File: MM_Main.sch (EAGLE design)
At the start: 81 parts, among them IC1 ULN2003AD, IC2 TB6612FNG, IC4 LD117ADT50TR, IC5 MCP1825, Q1 TEFT4300, Q2 TEFT4300, Q3 TEFT4300, Q4 TEFT4300, Q5 TEFT4300, Q6 TEFT4300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

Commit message: schamat kodu z CubeMX
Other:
- note added: "L"
- note added: "LF"
- note added: "LS"
- note added: "R"
- note added: "RF"
- note added: "RS"
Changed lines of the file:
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@@
 RF - Right Front
 </text>
+<text x="93.98" y="-48.26" size="1.778" layer="91">L</text>
+<text x="91.44" y="-48.26" size="1.778" layer="91">R</text>
+<text x="88.9" y="-45.72" size="1.778" layer="91" rot="R270">RF</text>
+<text x="86.36" y="-45.72" size="1.778" layer="91" rot="R270">RS</text>
+<text x="139.7" y="-17.78" size="1.778" layer="91">LS</text>
+<text x="109.22" y="-53.34" size="1.778" layer="91" rot="R90">LF</text>
 </plain>
 <instances>

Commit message: poprawione przyciski, kwarc i wylacznik zasilania
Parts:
- removed BT0, BT1, RST_BTN: TACTILE-SWITCH-7914G, GeekAmmo:TACTILE-SWITCH-7914G
- removed ZAS: (no value), special:SW_DIP-1
- added Q8: 8MHz, _microMouse:CRYSTAL_5X3.2MM
- added S1: TL32PO, switch:TL32PO
- added S2, S3: DTS-3, switch-tact:DTS-3
- added S4: DTSM-6, switch-tact:DTSM-6
- added S5: DTSM-3, switch-tact:DTSM-3
- added U$2: CRYSTAL_5X3.2MM, _microMouse:CRYSTAL_5X3.2MM
- C_OSC1, C_OSC2: value 27p -> 33p
- LED4: value green -> blue
- LED6: value yellow -> blue
- R10, R12, R13: value 10K -> 150R
- R11: value 10K -> 10k
- R20, R27: value 10K -> 33R
- R25: value (none) -> 10k
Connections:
- net +3V3: now also S3.1; no longer BT0.3
- net BTN: now also S2.1; no longer BT1.3
- net GND: now also S5.1; no longer RST_BTN.3
- net N$23: now also S3.2; no longer BT0.1
- net N$24: now also S1.P; no longer ZAS.2
- net N$29: now also S2.2; no longer BT1.1
- net N$9: now also S1.S; no longer ZAS.1
- net OSC_IN: now also Q8.2; no longer Q7.2
- net OSC_OUT: now also Q8.1; no longer Q7.1
- net RST: now also S5.2; no longer RST_BTN.1
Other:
- note removed: "L"
- note removed: "LF"
- note removed: "LS"
- note removed: "R"
- note removed: "RF"
- note removed: "RS"
- moved on the sheet: Q7

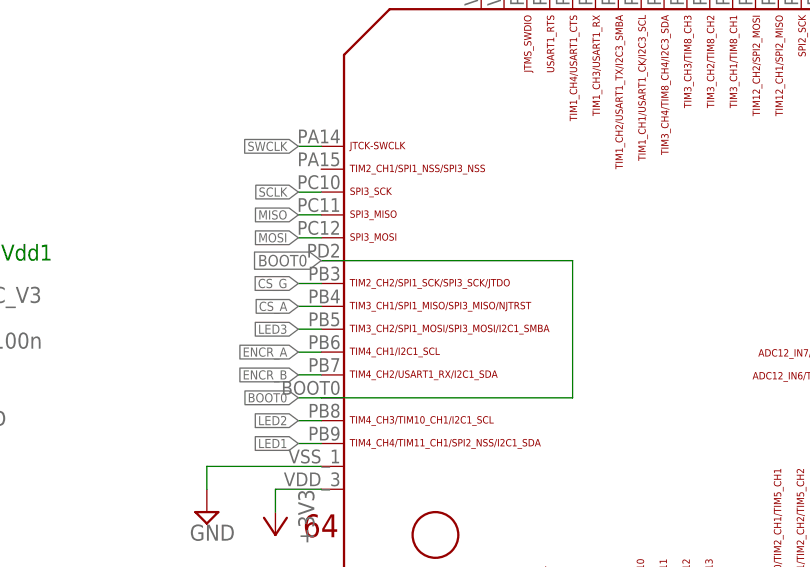
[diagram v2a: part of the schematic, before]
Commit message: PD2 zamienione z PA15
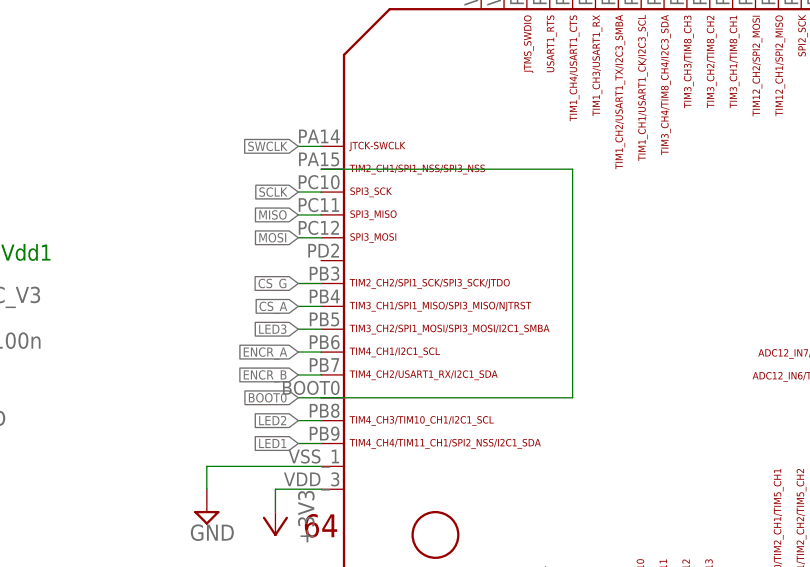
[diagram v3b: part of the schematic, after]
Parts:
- removed U$2: CRYSTAL_5X3.2MM, _microMouse:CRYSTAL_5X3.2MM
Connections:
- net BOOT0: now also U$6.PA15; no longer U$6.PD2
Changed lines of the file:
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@@
 <part name="+3V29" library="supply1" deviceset="+3V3" device=""/>
 <part name="R26" library="rcl" deviceset="R-EU_" device="R0805"/>
-<part name="U$2" library="_microMouse" deviceset="CRYSTAL_5X3.2MM" device=""/>
 <part name="Q8" library="_microMouse" deviceset="CRYSTAL_5X3.2MM" device="" value="8MHz"/>
 <part name="S1" library="switch" deviceset="TL32PO" device=""/>
@@
 <label x="48.26" y="-7.62" size="1.016" layer="95" rot="R180" xref="yes"/>
 <pinref part="U$6" gate="G$1" pin="BOOT0"/>
-<pinref part="U$6" gate="G$1" pin="PD2"/>
-<wire x1="50.8" y1="7.62" x2="78.74" y2="7.62" width="0.1524" layer="91"/>
-<wire x1="78.74" y1="7.62" x2="78.74" y2="-7.62" width="0.1524" layer="91"/>
 <wire x1="78.74" y1="-7.62" x2="50.8" y2="-7.62" width="0.1524" layer="91"/>
-<label x="50.8" y="7.62" size="1.27" layer="95" rot="R180" xref="yes"/>
-</segment>
-</net>
+<pinref part="U$6" gate="G$1" pin="PA15"/>
+<wire x1="78.74" y1="-7.62" x2="78.74" y2="17.78" width="0.1524" layer="91"/>
+<wire x1="78.74" y1="17.78" x2="50.8" y2="17.78" width="0.1524" layer="91"/>
+</segment>
+</net>

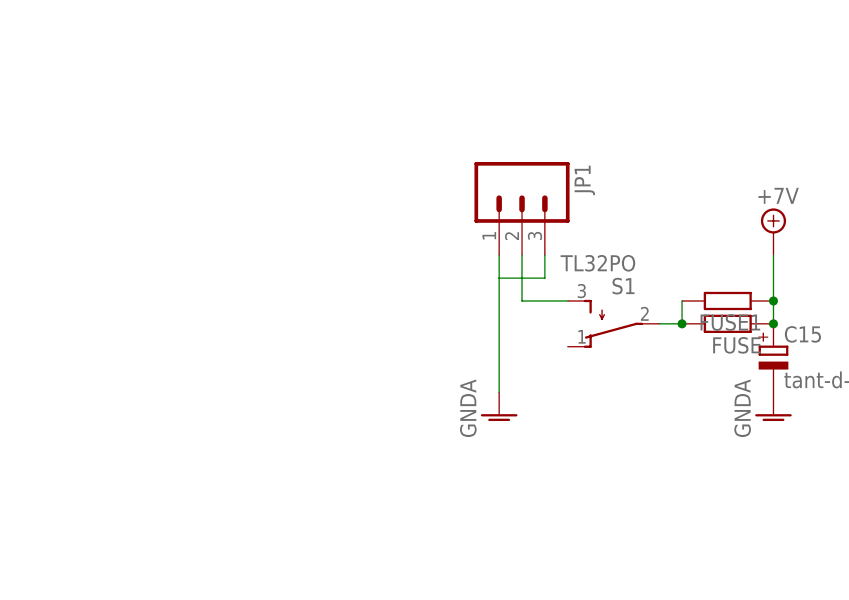
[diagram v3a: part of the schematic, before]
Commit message: dodany suwak i miejsce na 2 lipo
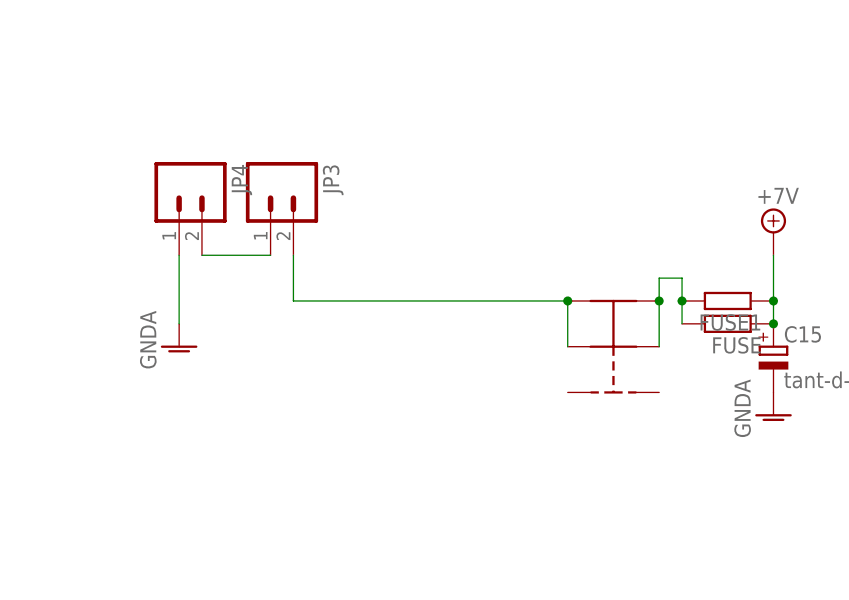
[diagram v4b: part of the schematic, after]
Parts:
- removed JP1: (no value), SparkFun-Connectors:M03POLAR
- removed S1: TL32PO, switch:TL32PO
- added JP3, JP4: (no value), SparkFun_conn:M02POLAR
- added U$3: PRZELACZNIK_SUWAKOWY, _microMouse:PRZELACZNIK_SUWAKOWY
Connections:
- new net N$36: JP3.2, U$3.2, U$3.3
- net GNDA: now also JP4.1; no longer JP1.1, JP1.3
- net N$24: now also U$3.5, U$3.6; no longer S1.P
- net N$9: now also JP3.1, JP4.2; no longer JP1.2, S1.S
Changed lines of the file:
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@@
 <part name="U$6" library="_microMouse" deviceset="STM32F4X5" device=""/>
 <part name="AGND1" library="supply2" deviceset="GND" device=""/>
-<part name="JP1" library="SparkFun-Connectors" deviceset="M03" device="POLAR"/>
 <part name="R15" library="rcl" deviceset="R-EU_" device="R0805"/>
 <part name="D2" library="_microMouse" deviceset="SFH4545" device="-C" value="SFH4545-C"/>
@@
 <part name="R26" library="rcl" deviceset="R-EU_" device="R0805"/>
 <part name="Q8" library="_microMouse" deviceset="CRYSTAL_5X3.2MM" device="" value="8MHz"/>
-<part name="S1" library="switch" deviceset="TL32PO" device=""/>
 <part name="S2" library="switch-tact" deviceset="DTS-3" device=""/>
 <part name="S3" library="switch-tact" deviceset="DTS-3" device=""/>
 <part name="S4" library="switch-tact" deviceset="DTSM-6" device=""/>
 <part name="S5" library="switch-tact" deviceset="DTSM-3" device=""/>
+<part name="JP3" library="SparkFun_conn" deviceset="M02" device="POLAR"/>
+<part name="JP4" library="SparkFun_conn" deviceset="M02" device="POLAR"/>
+<part name="U$3" library="_microMouse" deviceset="PRZELACZNIK_SUWAKOWY" device=""/>
 </parts>
 <sheets>
@@
 <instance part="+3V21" gate="G$1" x="0" y="10.16" smashed="yes"/>
 <instance part="+3V22" gate="G$1" x="-12.7" y="10.16" smashed="yes"/>
-<instance part="GND4" gate="1" x="-152.4" y="111.76"/>
+<instance part="GND4" gate="1" x="-187.96" y="119.38"/>
 <instance part="GND10" gate="1" x="-88.9" y="134.62"/>
 <instance part="AGND17" gate="GND" x="-78.74" y="134.62"/>
@@
 <instance part="U$6" gate="G$1" x="86.36" y="0"/>
 <instance part="AGND1" gate="GND" x="96.52" y="-50.8"/>
-<instance part="JP1" gate="G$1" x="-149.86" y="137.16" rot="R270"/>
 <instance part="R15" gate="G$1" x="86.36" y="154.94" rot="R90"/>
 <instance part="D2" gate="G$1" x="86.36" y="144.78"/>
@@
 <instance part="R26" gate="G$1" x="-165.1" y="30.48" rot="R180"/>
 <instance part="Q8" gate="G$1" x="-10.16" y="-25.4" rot="R90"/>
-<instance part="S1" gate="BEF1" x="-139.7" y="121.92" rot="R90"/>
 <instance part="S2" gate="G$1" x="-63.5" y="55.88" rot="R90"/>
 <instance part="S3" gate="G$1" x="205.74" y="30.48" rot="R180"/>
 <instance part="S4" gate="G$1" x="256.54" y="12.7"/>
 <instance part="S5" gate="G$1" x="238.76" y="15.24"/>
+<instance part="JP3" gate="G$1" x="-177.8" y="137.16" rot="R270"/>
+<instance part="JP4" gate="G$1" x="-187.96" y="137.16" rot="R270"/>
+<instance part="U$3" gate="G$1" x="-139.7" y="119.38" rot="R90"/>
 </instances>
 <busses>
@@
 </segment>
 <segment>
-<wire x1="-152.4" y1="127" x2="-152.4" y2="129.54" width="0.1524" layer="91"/>
-<wire x1="-152.4" y1="127" x2="-147.32" y2="127" width="0.1524" layer="91"/>
-<wire x1="-147.32" y1="127" x2="-147.32" y2="129.54" width="0.1524" layer="91"/>
-<wire x1="-152.4" y1="127" x2="-152.4" y2="114.3" width="0.1524" layer="91"/>
 <pinref part="GND4" gate="1" pin="GNDA"/>
-<pinref part="JP1" gate="G$1" pin="1"/>
-<pinref part="JP1" gate="G$1" pin="3"/>
+<pinref part="JP4" gate="G$1" pin="1"/>
+<wire x1="-187.96" y1="121.92" x2="-187.96" y2="129.54" width="0.1524" layer="91"/>
 </segment>
 <segment>
@@
 <pinref part="FUSE" gate="G$1" pin="2"/>
 <pinref part="FUSE1" gate="G$1" pin="2"/>
-<pinref part="S1" gate="BEF1" pin="P"/>
-<wire x1="-132.08" y1="121.92" x2="-134.62" y2="121.92" width="0.1524" layer="91"/>
-<junction x="-132.08" y="121.92"/>
+<wire x1="-132.08" y1="124.46" x2="-132.08" y2="127" width="0.1524" layer="91"/>
+<wire x1="-132.08" y1="127" x2="-134.62" y2="127" width="0.1524" layer="91"/>
+<junction x="-132.08" y="124.46"/>
+<pinref part="U$3" gate="G$1" pin="6"/>
+<pinref part="U$3" gate="G$1" pin="5"/>
+<wire x1="-134.62" y1="124.46" x2="-134.62" y2="119.38" width="0.1524" layer="91"/>
+<wire x1="-134.62" y1="127" x2="-134.62" y2="124.46" width="0.1524" layer="91"/>
+<junction x="-134.62" y="124.46"/>
 </segment>
 </net>
@@
 </segment>
 </net>
-<net name="N$9" class="0">
-<segment>
-<wire x1="-149.86" y1="129.54" x2="-149.86" y2="124.46" width="0.1524" layer="91"/>
-<pinref part="JP1" gate="G$1" pin="2"/>
-<pinref part="S1" gate="BEF1" pin="S"/>
-<wire x1="-144.78" y1="124.46" x2="-149.86" y2="124.46" width="0.1524" layer="91"/>
-</segment>
-</net>
 <net name="INT_A" class="0">
 <segment>
@@
 </segment>
 </net>
+<net name="N$36" class="0">
+<segment>
+<pinref part="U$3" gate="G$1" pin="2"/>
+<pinref part="U$3" gate="G$1" pin="3"/>
+<wire x1="-144.78" y1="119.38" x2="-144.78" y2="124.46" width="0.1524" layer="91"/>
+<wire x1="-175.26" y1="124.46" x2="-144.78" y2="124.46" width="0.1524" layer="91"/>
+<junction x="-144.78" y="124.46"/>
+<pinref part="JP3" gate="G$1" pin="2"/>
+<wire x1="-175.26" y1="129.54" x2="-175.26" y2="124.46" width="0.1524" layer="91"/>
+</segment>
+</net>
+<net name="N$9" class="0">
+<segment>
+<pinref part="JP3" gate="G$1" pin="1"/>
+<pinref part="JP4" gate="G$1" pin="2"/>
+<wire x1="-177.8" y1="129.54" x2="-185.42" y2="129.54" width="0.1524" layer="91"/>
+</segment>
+</net>

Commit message: gerbery
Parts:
- removed Q7: 8MHz, crystal:CRYSTALCTS406
- removed S4: DTSM-6, switch-tact:DTSM-6
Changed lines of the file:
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@@
 <part name="C_V1" library="rcl" deviceset="C-EU" device="C0805" value="100n"/>
 <part name="C_V2" library="rcl" deviceset="C-EU" device="C0805" value="100n"/>
-<part name="Q7" library="crystal" deviceset="CRYSTAL" device="CTS406" value="8MHz"/>
 <part name="C_OSC1" library="rcl" deviceset="C-EU" device="C0805" value="33p"/>
 <part name="C_OSC2" library="rcl" deviceset="C-EU" device="C0805" value="33p"/>
@@
 <part name="S2" library="switch-tact" deviceset="DTS-3" device=""/>
 <part name="S3" library="switch-tact" deviceset="DTS-3" device=""/>
-<part name="S4" library="switch-tact" deviceset="DTSM-6" device=""/>
 <part name="S5" library="switch-tact" deviceset="DTSM-3" device=""/>
 <part name="JP3" library="SparkFun_conn" deviceset="M02" device="POLAR"/>
@@
 <instance part="C_V1" gate="G$1" x="0" y="2.54"/>
 <instance part="C_V2" gate="G$1" x="-12.7" y="2.54"/>
-<instance part="Q7" gate="G$1" x="-2.54" y="-25.4" smashed="yes" rot="R90">
-<attribute name="NAME" x="-3.556" y="-21.844" size="1.778" layer="95" rot="R180"/>
-<attribute name="VALUE" x="7.112" y="-24.638" size="1.778" layer="96" rot="R180"/>
-</instance>
 <instance part="C_OSC1" gate="G$1" x="-17.78" y="-20.32" smashed="yes" rot="R90">
 <attribute name="NAME" x="-9.144" y="-15.621" size="1.778" layer="95" rot="R180"/>
@@
 <instance part="S2" gate="G$1" x="-63.5" y="55.88" rot="R90"/>
 <instance part="S3" gate="G$1" x="205.74" y="30.48" rot="R180"/>
-<instance part="S4" gate="G$1" x="256.54" y="12.7"/>
 <instance part="S5" gate="G$1" x="238.76" y="15.24"/>
 <instance part="JP3" gate="G$1" x="-177.8" y="137.16" rot="R270"/>

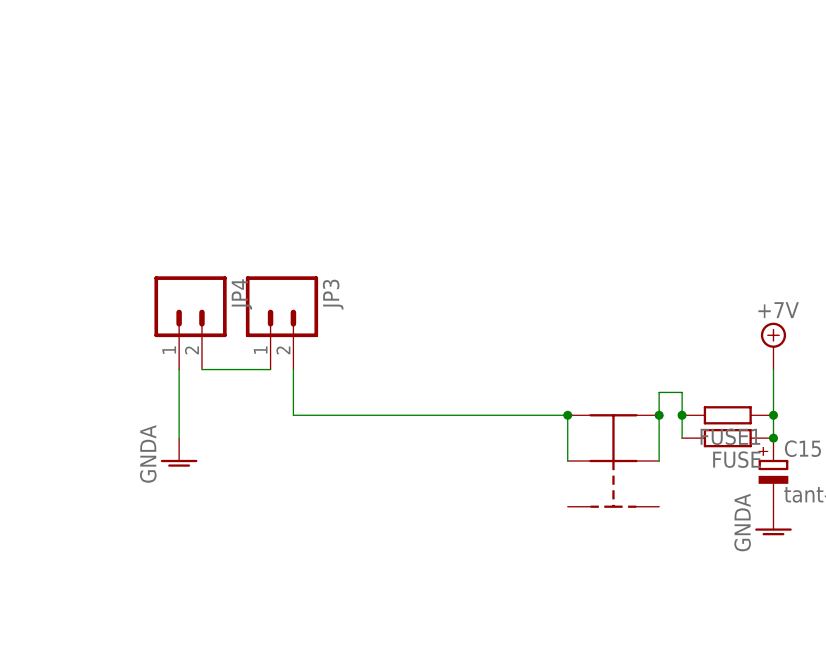
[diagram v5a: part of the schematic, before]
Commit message: to 2 gniazdo moze szorowac o kolo... zmienilem tez konfiguuracje power-switcha, bo tak patrzac na strone electro-parku to tak odczyruje ta konfiguracje, zrobilem drc
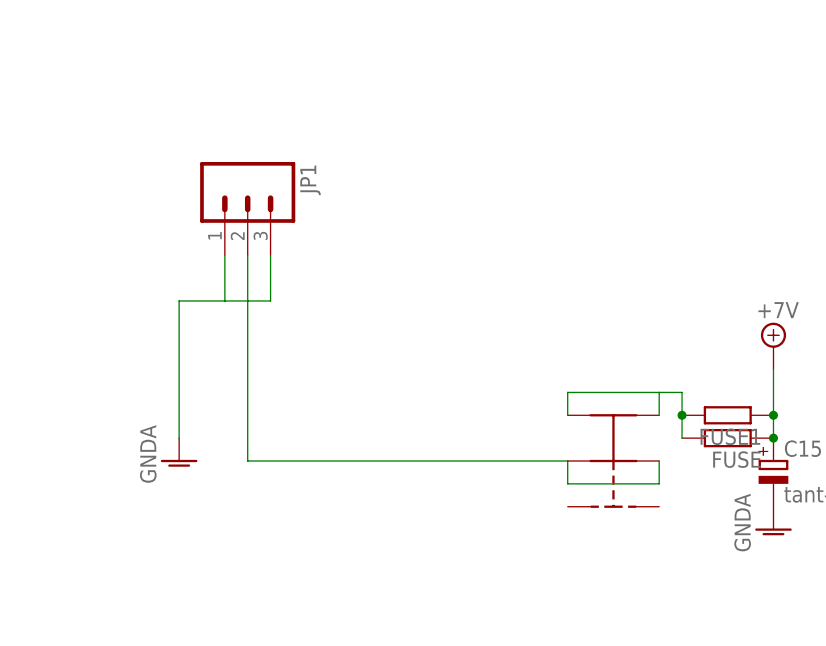
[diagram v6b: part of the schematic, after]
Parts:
- removed JP3, JP4: (no value), SparkFun_conn:M02POLAR
- added JP1: (no value), SparkFun-Connectors:M03POLAR
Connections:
- removed net N$9: JP3.1, JP4.2
- net GNDA: now also JP1.1, JP1.3; no longer JP4.1
- net N$24: now also U$3.3; no longer U$3.5
- net N$36: now also JP1.2, U$3.5; no longer JP3.2, U$3.3

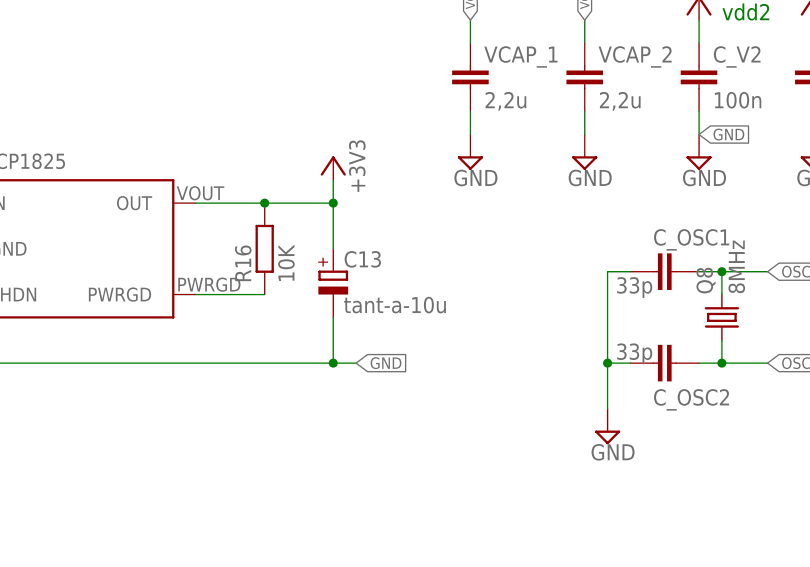
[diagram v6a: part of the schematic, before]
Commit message: wywalilem elementy ktore byly pod podstawka silnika
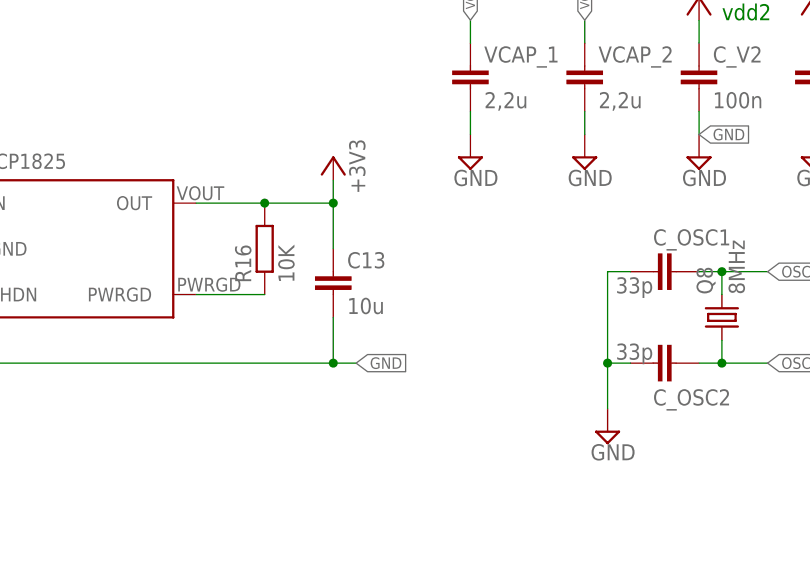
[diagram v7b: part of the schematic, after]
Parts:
- C13: value tant-a-10u -> 10u; device rcl:CPOL-EUSMCA -> rcl:C-EUC0805
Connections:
- net +3V3: now also C13.1; no longer C13.+
- net GND: now also C13.2; no longer C13.-

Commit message: poprawione piny w cubemx
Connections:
- net ADC_PA3 renamed ADC_LS
- net N$13 renamed SENSOR_LS
- net N$14 renamed SENSOR_RS
- net N$15 renamed SENSOR_R
- net N$16 renamed SENSOR_RF
- net N$2 renamed SENSOR_LF
- net N$33 renamed SENSOR_L
- removed net ADC_PA2: Q2.E, R23.2, U$6.PA2
- new net ADC_RS: Q6.E, R1.2, U$6.PC0
- net ADC_L: now also Q3.E, R4.2, U$6.PC3; no longer Q5.E, R2.2, U$6.PC1
- net ADC_LF: now also Q2.E, R23.2, U$6.PA2; no longer Q6.E, R1.2, U$6.PC0
- net ADC_RF: now also Q5.E, R2.2, U$6.PC1; no longer Q3.E, R4.2, U$6.PC3
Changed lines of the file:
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@@
 </busses>
 <nets>
-<net name="ADC_RF" class="0">
+<net name="ADC_L" class="0">
 <segment>
 <pinref part="Q3" gate="G$1" pin="E"/>
@@
 </segment>
 </net>
-<net name="ADC_L" class="0">
+<net name="ADC_RF" class="0">
 <segment>
 <pinref part="Q5" gate="G$1" pin="E"/>
@@
 </segment>
 </net>
-<net name="ADC_LF" class="0">
+<net name="ADC_RS" class="0">
 <segment>
 <pinref part="Q6" gate="G$1" pin="E"/>
@@
 </segment>
 </net>
-<net name="N$16" class="0">
+<net name="SENSOR_RF" class="0">
 <segment>
 <pinref part="D5" gate="G$1" pin="C"/>
@@
 </segment>
 </net>
-<net name="N$2" class="0">
+<net name="SENSOR_LF" class="0">
 <segment>
 <pinref part="D2" gate="G$1" pin="C"/>
@@
 </segment>
 </net>
-<net name="ADC_PA2" class="0">
+<net name="ADC_LF" class="0">
 <segment>
 <pinref part="Q2" gate="G$1" pin="E"/>
@@
 </segment>
 </net>
-<net name="ADC_PA3" class="0">
+<net name="ADC_LS" class="0">
 <segment>
 <pinref part="Q1" gate="G$1" pin="E"/>
@@
 </segment>
 </net>
-<net name="N$13" class="0">
+<net name="SENSOR_LS" class="0">
 <segment>
 <pinref part="D1" gate="G$1" pin="C"/>
@@
 </segment>
 </net>
-<net name="N$14" class="0">
+<net name="SENSOR_RS" class="0">
 <segment>
 <pinref part="D6" gate="G$1" pin="C"/>
@@
 </segment>
 </net>
-<net name="N$15" class="0">
+<net name="SENSOR_R" class="0">
 <segment>
 <pinref part="D4" gate="G$1" pin="C"/>
@@
 </segment>
 </net>
-<net name="N$33" class="0">
+<net name="SENSOR_L" class="0">
 <segment>
 <pinref part="IC1" gate="A" pin="O3"/>
